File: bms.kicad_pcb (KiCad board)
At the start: 4 copper layers, 100 x 67 mm, 178 parts, among them J1 CELL_TAPS, J2 I2C_IN, J3 THERM_1, J4 THERM_2, J5 SWD, Q1 AO3400A, Q10 AO3400A, Q11 AO3400A, Q12 AO3400A, Q13 AO3400A, Q14 AO3400A, Q15 AO3400A, Q16 AO3400A, Q17 AO3400A, Q18 AO3400A, Q19 AO3400A, Q2 AO3400A, Q20 AO3400A, Q3 AO3400A, Q4 AO3400A, Q5 AO3400A, Q6 AO3400A, Q7 AO3400A, Q8 AO3400A, Q9 AO3400A, SW1 SW_Push, U1 LMR516xx, U2 STM32F103C8Tx, U3 ADuM1252, U4 MAX14920, U5 MAX11163, U6 REF61xx, Y1 8M

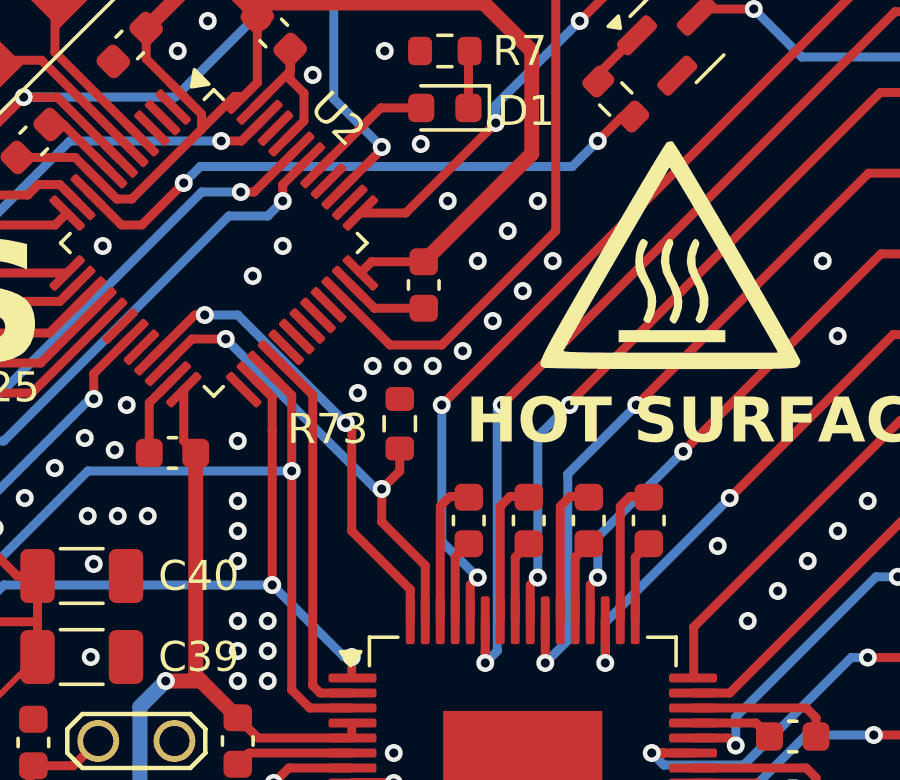
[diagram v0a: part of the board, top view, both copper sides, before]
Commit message: *: Add solder jumpers for I2C address select
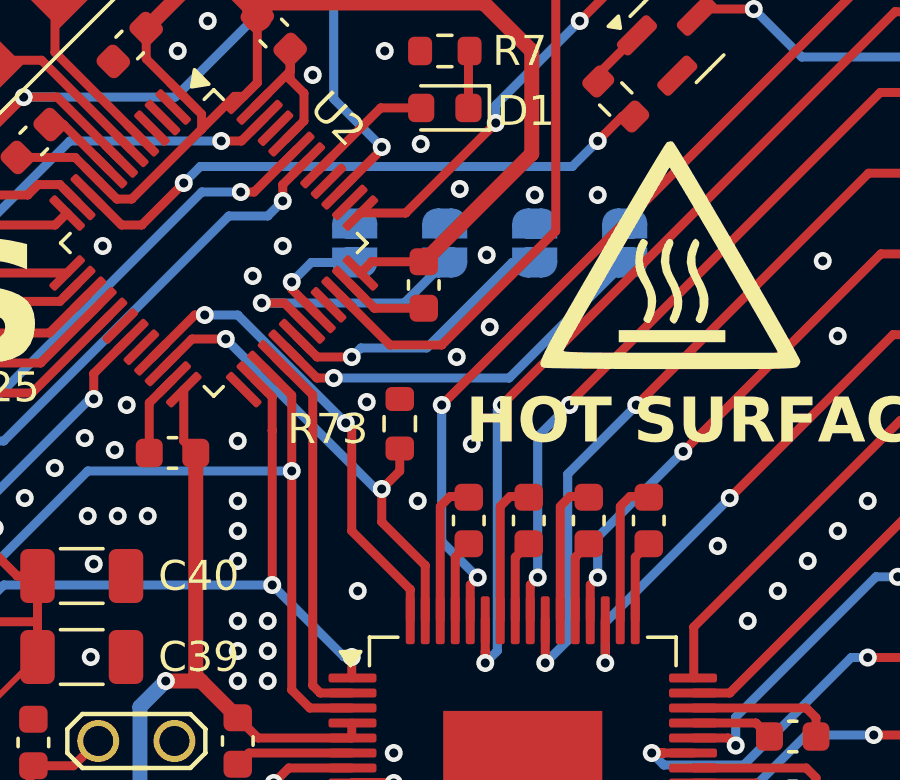
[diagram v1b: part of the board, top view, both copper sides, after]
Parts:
- added JP1: SolderJumper_2_Open, Jumper:SolderJumper-2_P1.3mm_Open_RoundedPad1.0x1.5mm, B.Cu at (99.9, 69.4)
- added JP2: SolderJumper_2_Open, Jumper:SolderJumper-2_P1.3mm_Open_RoundedPad1.0x1.5mm, B.Cu at (96.9, 69.4)
- added JP3: SolderJumper_2_Open, Jumper:SolderJumper-2_P1.3mm_Open_RoundedPad1.0x1.5mm, B.Cu at (93.9, 69.4)
- added JP4: SolderJumper_2_Open, Jumper:SolderJumper-2_P1.3mm_Open_RoundedPad1.0x1.5mm, B.Cu at (90.9, 69.4)
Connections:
- U2 pad 29: unconnected-(U2-PA8-Pad29) -> Net-(JP1-B)
- U2 pad 30: unconnected-(U2-PA9-Pad30) -> Net-(JP2-B)
- U2 pad 31: unconnected-(U2-PA10-Pad31) -> Net-(JP3-B)
- U2 pad 32: unconnected-(U2-PA11-Pad32) -> Net-(JP4-B)
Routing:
- net Net-(JP1-B): track 0.00 -> 13.4 mm, vias 0 -> 1
- net Net-(JP2-B): track 0.00 -> 9.52 mm, vias 0 -> 1
- net Net-(JP3-B): track 0.00 -> 8.50 mm, vias 0 -> 1
- net Net-(JP4-B): track 0.00 -> 3.84 mm, vias 0 -> 1
- net GND: vias 658 -> 656
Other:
- board text added: "1"
- board text added: "2"
- board text added: "3"
- board text added: "4"

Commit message: pcb: Improve I2C address select silkscreen
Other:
- board text added: "A0"
- board text added: "A1"
- board text added: "A2"
- board text added: "A3"
- board text removed: "1"
- board text removed: "2"
- board text removed: "3"
- board text removed: "4"

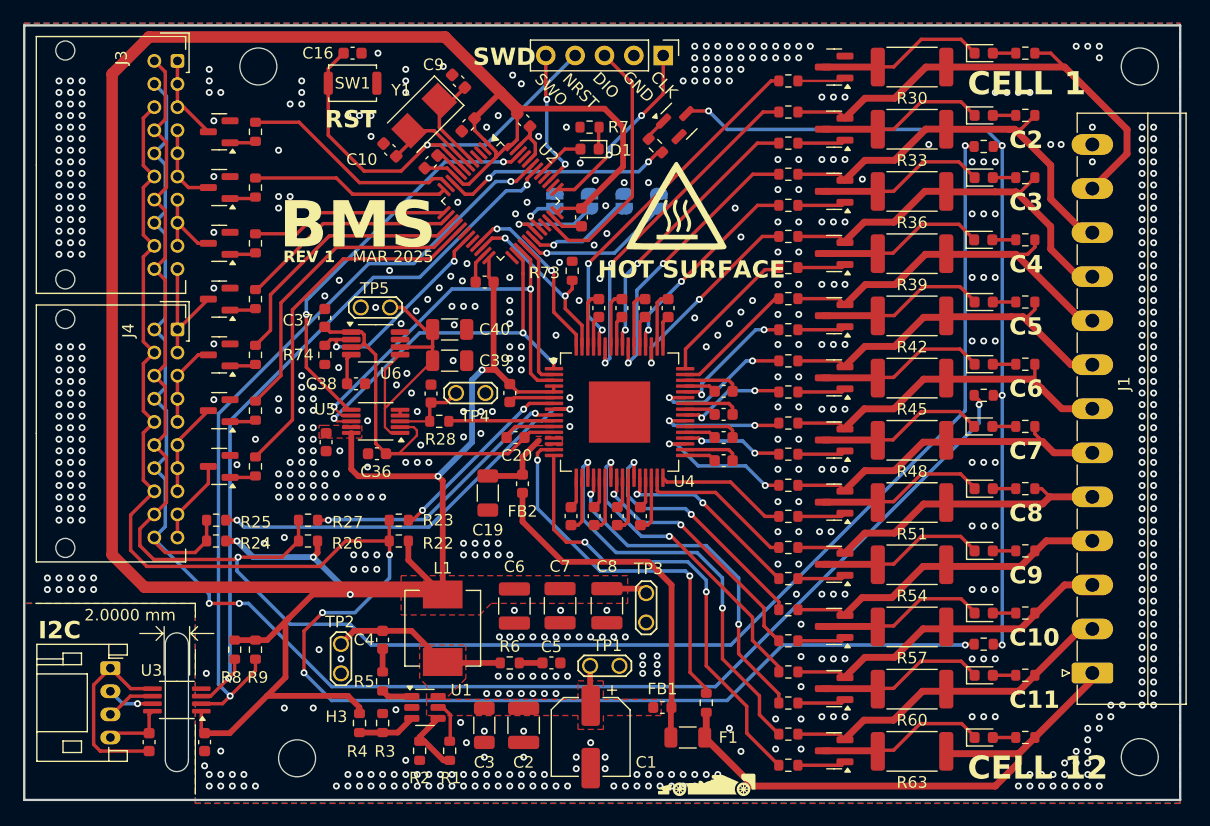
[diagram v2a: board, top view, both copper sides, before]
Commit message: pcb: Move some tracks and vias to reduce missing ground fill
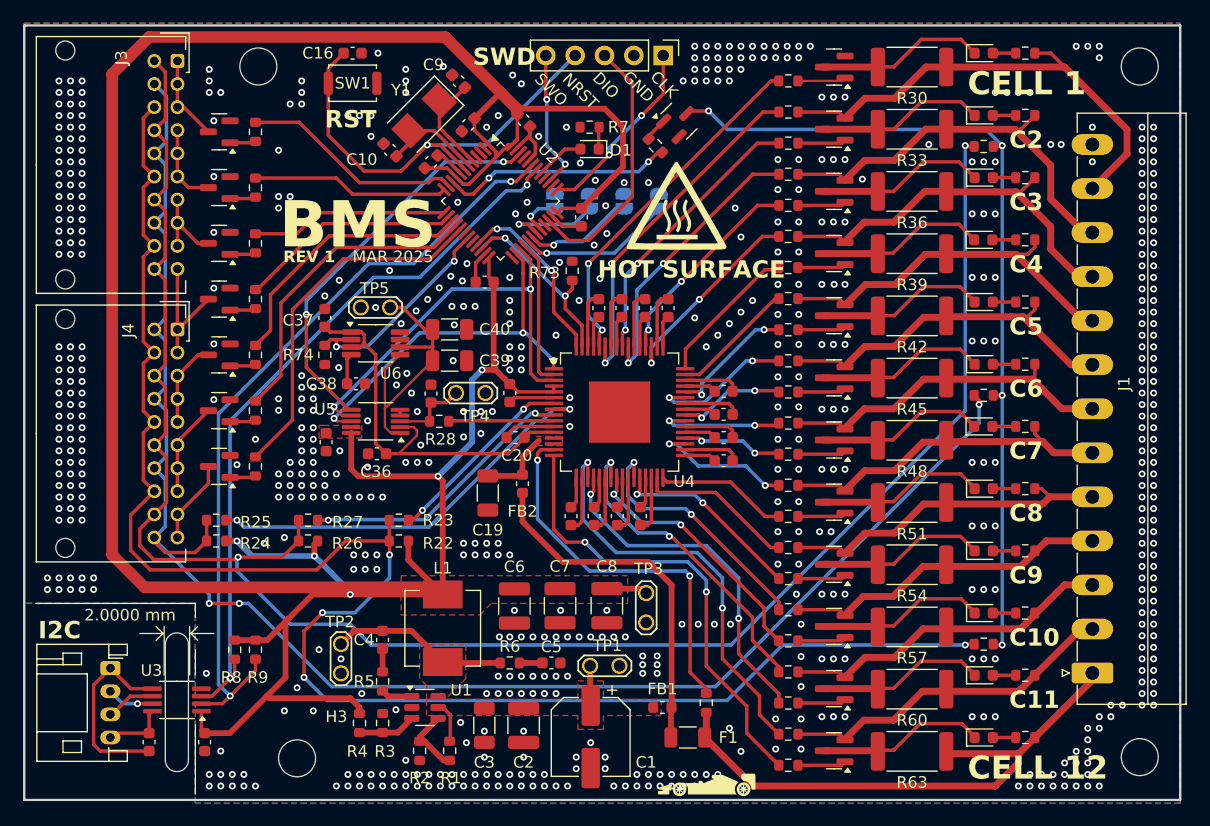
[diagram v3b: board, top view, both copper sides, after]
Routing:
- net Net-(U4-CV12): track 32.7 -> 33.2 mm
- net GND: vias 656 -> 661

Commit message: schematic: Update value for buck converter bootstrap resistor
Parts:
- R5: value 0 -> 6R8
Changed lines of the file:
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@@
 			)
 		)
-		(property "Value" "0"
+		(property "Value" "6R8"
 			(at 0 1.43 270)
 			(layer "F.Fab")
